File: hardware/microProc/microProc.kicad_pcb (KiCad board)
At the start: 2 copper layers, 23 parts, among them J1 POWER, J2 INPUT, J3 OUTPUT, J4 Conn_02x07_Odd_Even, U1 STM32L021K4Tx, U2 BU33SD5WG-TR, U3 MCP4801

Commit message: Component placement
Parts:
- added H1: MountingHole_Pad, MountingHole:MountingHole_3.2mm_M3_Pad, F.Cu at (107.0, 55.0)
- added H2: MountingHole_Pad, MountingHole:MountingHole_3.2mm_M3_Pad, F.Cu at (157.0, 55.0)
- added H3: MountingHole_Pad, MountingHole:MountingHole_3.2mm_M3_Pad, F.Cu at (157.0, 95.0)
- added H4: MountingHole_Pad, MountingHole:MountingHole_3.2mm_M3_Pad, F.Cu at (107.0, 95.0)
- moved D2 60.1 mm to (120.1, 63.0), turned to 180 degrees
- moved U2 57.9 mm to (120.0, 55.0), turned to 180 degrees
- moved C8 57.4 mm to (119.9, 59.7)
- moved C7 57.3 mm to (125.3, 55.0), turned to 90 degrees
- moved R3 52.9 mm to (125.3, 62.0), turned to 90 degrees
- moved R2 43.2 mm to (131.7, 66.7)
- moved J3 37.4 mm to (157.0, 76.0), turned to 90 degrees
- moved L1 36.9 mm to (121.0, 73.0), turned to 90 degrees
- moved C3 33.0 mm to (127.0, 69.0), turned to 90 degrees
- moved C6 32.4 mm to (121.0, 78.0), turned to -90 degrees
- moved U1 28.9 mm to (132.0, 75.0)
- moved J1 27.9 mm to (131.0, 55.0)
- moved C5 27.9 mm to (124.0, 78.0), turned to -90 degrees
- moved D1 27.9 mm to (142.2, 77.0), turned to 180 degrees
- moved C4 26.7 mm to (124.0, 73.3), turned to 90 degrees
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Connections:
- D1 pad 1: LED_STATUS -> Net-(R1-Pad1)
- D1 pad 2: Net-(D1-Pad2) -> LED_STATUS
- R1 pad 1: Net-(D1-Pad2) -> Net-(R1-Pad1)
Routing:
- added copper zone on B.Cu, net GND
- added copper zone on F.Cu, net GND
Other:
- board outline added: 58 x 48.1 mm

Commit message: Routage carte
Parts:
- moved C10 11.7 mm to (140.0, 86.2), turned to -90 degrees
- moved C9 7.79 mm to (137.2, 86.2), turned to -90 degrees
- moved C1 4.01 mm to (142.5, 80.6)
- moved R1 4.00 mm to (146.0, 74.0), turned to 0 degrees
- moved D1 1.85 mm to (144.0, 77.0)
- moved U3 1.51 mm to (130.5, 86.2), turned to 180 degrees
- moved C2 0.52 mm to (139.5, 80.6), turned to -90 degrees
- turned C7 to 180 degrees
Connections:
- C8 pad 1: +3V3 -> +3.3V
- D2 pad 2: +3V3 -> +3.3V
- U2 pad 5: +3V3 -> +3.3V
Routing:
- net +3.3V: track 0.00 -> 105.4 mm
- net DAC_OUT: track 0.00 -> 35.8 mm
- net ADC_IN1: track 0.00 -> 26.6 mm
- net NRST: track 0.00 -> 25.0 mm, vias 0 -> 2
- net USART2_RX: track 0.00 -> 23.1 mm, vias 0 -> 2
- net USART2_TX: track 0.00 -> 22.4 mm, vias 0 -> 2
- net +5V: track 0.00 -> 21.1 mm
- net SWDIO: track 0.00 -> 16.6 mm
- net SWDCK: track 0.00 -> 15.1 mm
- net LED_STATUS: track 0.00 -> 14.1 mm
- net +3.3VA: track 0.00 -> 10.3 mm
- net DAC_nCS: track 0.00 -> 9.74 mm
- net SPI1_SCK: track 0.00 -> 8.12 mm
- net Net-(R2-Pad1): track 0.00 -> 7.92 mm
- net SPI1_MOSI: track 0.00 -> 6.45 mm
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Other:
- rule pad_to_mask_clearance: 0 -> 0.1

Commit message: Final Final PCB
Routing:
- net GND: track 3.11 -> 6.88 mm

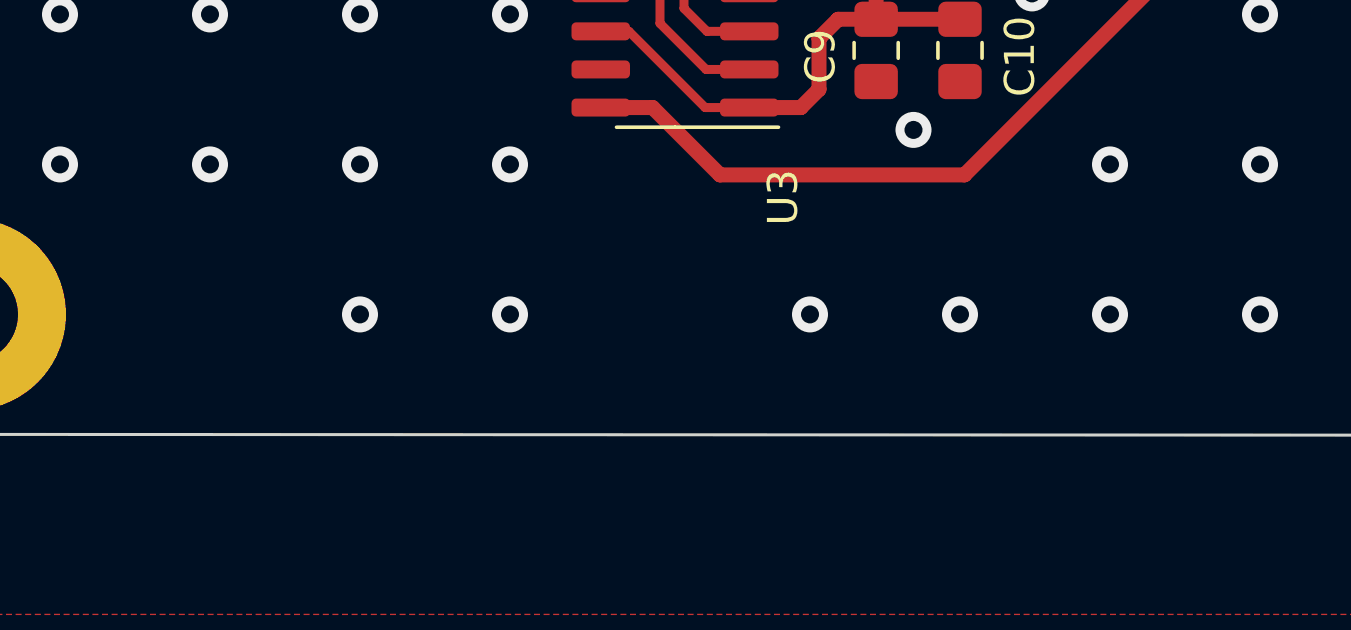
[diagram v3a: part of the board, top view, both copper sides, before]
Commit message: Added names to PCB
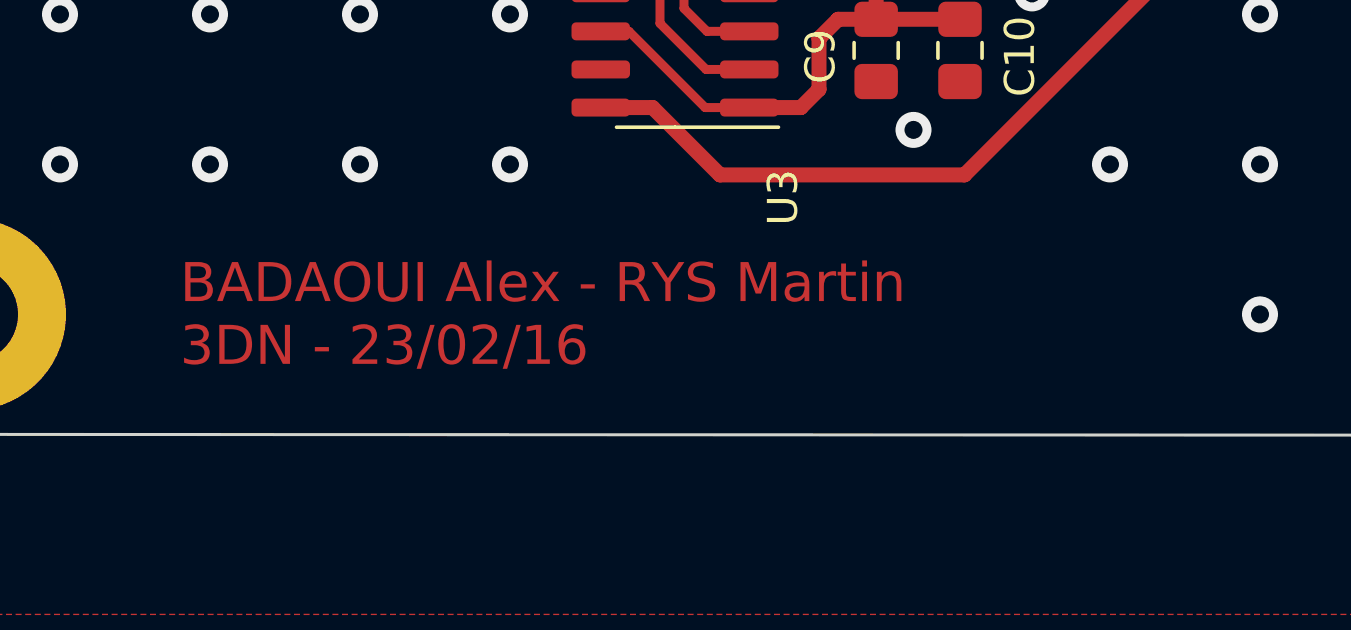
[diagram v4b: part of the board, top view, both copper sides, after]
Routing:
- net GND: vias 57 -> 52
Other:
- board text added: "BADAOUI Alex - RYS Martin 3DN - 23/02/16"
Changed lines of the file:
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@@
   (gr_line (start 160.999999 94.5) (end 161 55) (layer "Edge.Cuts") (width 0.1))
   (gr_arc (start 103 55) (mid 104.125185 52.09575) (end 107 50.897357) (layer "Edge.Cuts") (width 0.1))
+  (gr_text "BADAOUI Alex - RYS Martin \n3DN - 23/02/16" (at 114 95) (layer "F.Cu")
+    (effects (font (size 1.3 1.3) (thickness 0.3)) (justify left))
+  )
   (segment (start 132 65) (end 140 57) (width 0.5) (layer "F.Cu") (net 1))
   (segment (start 134.2 73.5) (end 133.5 72.8) (width 0.5) (layer "F.Cu") (net 1))
@@
   (via (at 115 90) (size 1.2) (drill 0.6) (layers "F.Cu" "B.Cu") (free) (net 2))
   (via (at 120 85) (size 1.2) (drill 0.6) (layers "F.Cu" "B.Cu") (free) (net 2))
-  (via (at 140 95) (size 1.2) (drill 0.6) (layers "F.Cu" "B.Cu") (free) (net 2))
-  (via (at 120 95) (size 1.2) (drill 0.6) (layers "F.Cu" "B.Cu") (free) (net 2))
   (via (at 110 65) (size 1.2) (drill 0.6) (layers "F.Cu" "B.Cu") (free) (net 2))
   (via (at 150 75) (size 1.2) (drill 0.6) (layers "F.Cu" "B.Cu") (free) (net 2))
@@
   (via (at 115 70) (size 1.2) (drill 0.6) (layers "F.Cu" "B.Cu") (free) (net 2))
   (via (at 130 60) (size 1.2) (drill 0.6) (layers "F.Cu" "B.Cu") (free) (net 2))
-  (via (at 145 95) (size 1.2) (drill 0.6) (layers "F.Cu" "B.Cu") (free) (net 2))
   (via (at 145 55) (size 1.2) (drill 0.6) (layers "F.Cu" "B.Cu") (free) (net 2))
   (via (at 137 63) (size 1.2) (drill 0.6) (layers "F.Cu" "B.Cu") (free) (net 2))
@@
   (via (at 127 82) (size 1.2) (drill 0.6) (layers "F.Cu" "B.Cu") (free) (net 2))
   (via (at 123 56.5) (size 1.2) (drill 0.6) (layers "F.Cu" "B.Cu") (free) (net 2))
-  (via (at 125 95) (size 1.2) (drill 0.6) (layers "F.Cu" "B.Cu") (free) (net 2))
   (via (at 150 95) (size 1.2) (drill 0.6) (layers "F.Cu" "B.Cu") (free) (net 2))
   (via (at 120 90) (size 1.2) (drill 0.6) (layers "F.Cu" "B.Cu") (free) (net 2))
@@
   (via (at 150 90) (size 1.2) (drill 0.6) (layers "F.Cu" "B.Cu") (free) (net 2))
   (via (at 120 66.8) (size 1.2) (drill 0.6) (layers "F.Cu" "B.Cu") (free) (net 2))
-  (via (at 135 95) (size 1.2) (drill 0.6) (layers "F.Cu" "B.Cu") (free) (net 2))
   (via (at 155 65) (size 1.2) (drill 0.6) (layers "F.Cu" "B.Cu") (free) (net 2))
   (via (at 115 75) (size 1.2) (drill 0.6) (layers "F.Cu" "B.Cu") (free) (net 2))
